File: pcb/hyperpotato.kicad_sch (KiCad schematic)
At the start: 60 parts, among them J1 Conn_01x02_Socket, J2 Conn_01x02_Socket, J3 Conn_01x04, J4 Conn_01x04, J6 Conn_01x12_Socket, K1 SW_Push, K10 SW_Push, K11 SW_Push, K12 SW_Push, K13 SW_Push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

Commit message: WIP re-layout
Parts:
- K1, K10, K11, K12, K13, K14, K16, K17, K2, K3, K4, K6, K7, K8: footprint hyperpotato:PG1350_HS_reversible_plated -> hyperpotato:V1_V2_HS_reversible_plated; symbol Switch:SW_Push -> hyperpotato:SW_Push
- K15: footprint hyperpotato:PG1350_HS_reversible_plated -> hyperpotato:V1_V2_HS_reversible_plated_alt; symbol Switch:SW_Push -> hyperpotato:SW_Push
- K5, K9: footprint hyperpotato:PG1350_reversible_side -> hyperpotato:V1_V2_HS_reversible_plated; symbol Switch:SW_Push -> hyperpotato:SW_Push
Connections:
- net COL3: now also K9.1; no longer K9.2
- net COL4: now also K15.2; no longer K15.1
- net ROW0: now also K1.3, K2.3, K3.3, K4.3, K5.3
- net ROW1: now also K10.3, K6.3, K7.3, K8.3, K9.3
- net ROW2: now also K11.3, K12.3, K13.3, K14.3, K15.3
- net ROW3: now also K16.3, K17.3
- net TP_CLK: now also J6.8 (Pin_8); no longer J6.6 (Pin_6)
- net TP_DATA: now also J6.2 (Pin_2); no longer J6.1 (Pin_1)
- net TP_PCB_RESET: now also J6.3 (Pin_3); no longer J6.2 (Pin_2)
- net VCC: now also J6.1 (Pin_1); no longer J6.8 (Pin_8)
- net at D15.2 (A): now also K15.1; no longer K15.2
- net at D9.2 (A): now also K9.2; no longer K9.1

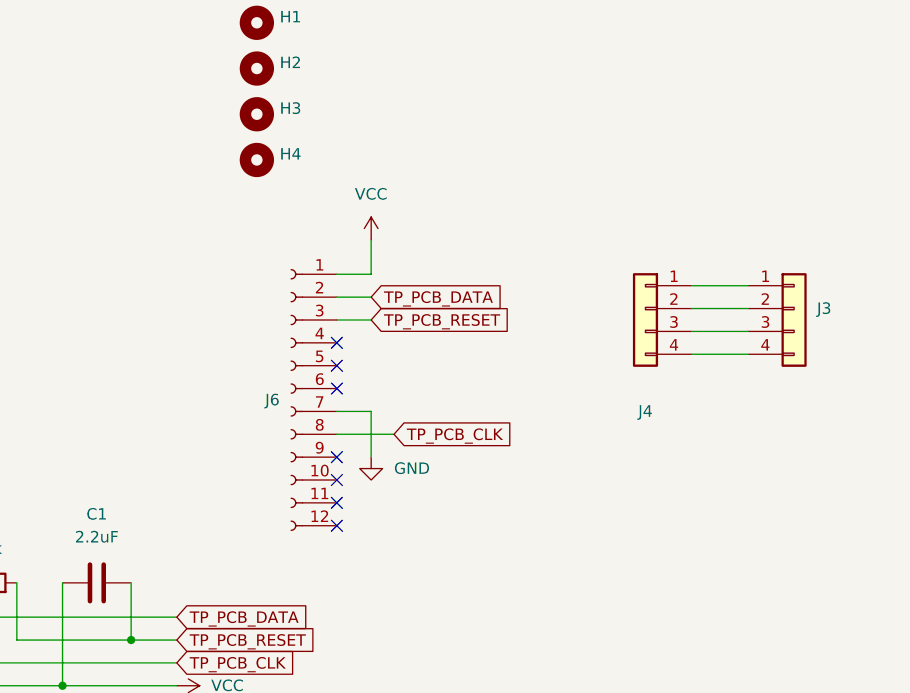
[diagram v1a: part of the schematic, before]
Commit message: WIP trackpoint mounting
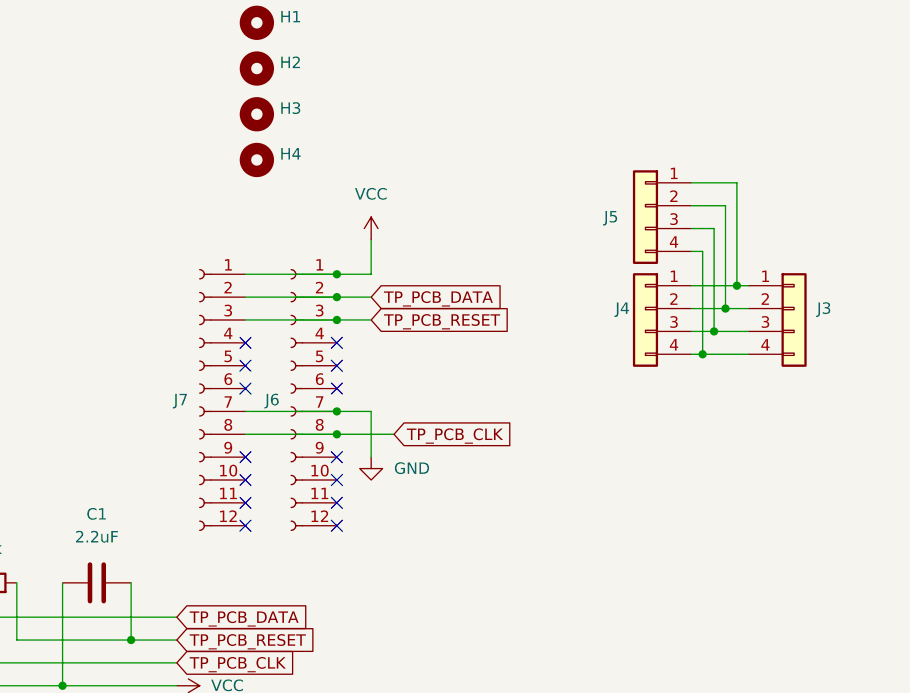
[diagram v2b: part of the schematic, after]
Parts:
- added J5: Conn_01x04, hyperpotato:Trackpoint_Connector, symbol Connector_Generic:Conn_01x04
- added J7: Conn_01x12_Socket, hyperpotato:Trackpoint_PCB_Connector, symbol Connector:Conn_01x12_Socket
- J3: footprint hyperpotato:Trackpoint_Connector -> hyperpotato:Trackpoint_Connector_Reversible
- J4: footprint hyperpotato:Trackponit_PCB -> hyperpotato:Trackpoint_Connector
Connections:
- net GND: now also J7.7 (Pin_7)
- net TP_CLK: now also J7.8 (Pin_8)
- net TP_DATA: now also J7.2 (Pin_2)
- net TP_PCB_RESET: now also J7.3 (Pin_3)
- net VCC: now also J7.1 (Pin_1)
- net at J3.1 (Pin_1), J4.1 (Pin_1): now also J5.1 (Pin_1)
- net at J3.2 (Pin_2), J4.2 (Pin_2): now also J5.2 (Pin_2)
- net at J3.3 (Pin_3), J4.3 (Pin_3): now also J5.3 (Pin_3)
- net at J3.4 (Pin_4), J4.4 (Pin_4): now also J5.4 (Pin_4)
- no-connect marks 10 -> 17
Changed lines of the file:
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@@
 (kicad_sch (version 20230121) (generator eeschema)
   (paper "A4")
+  (junction (at 100.33 149.86) (diameter 0) (color 0 0 0 0)
+  )
   (junction (at 245.11 41.91) (diameter 0) (color 0 0 0 0)
   )
   (junction (at 68.58 48.26) (diameter 0) (color 0 0 0 0)
   )
+  (junction (at 100.33 144.78) (diameter 0) (color 0 0 0 0)
+  )
   (junction (at 86.36 78.74) (diameter 0) (color 0 0 0 0)
   )
@@
   (junction (at 81.28 60.96) (diameter 0) (color 0 0 0 0)
   )
+  (junction (at 140.97 153.67) (diameter 0) (color 0 0 0 0)
+  )
   (junction (at 73.66 40.64) (diameter 0) (color 0 0 0 0)
   )
+  (junction (at 144.78 146.05) (diameter 0) (color 0 0 0 0)
+  )
   (junction (at 40.64 53.34) (diameter 0) (color 0 0 0 0)
   )
@@
   (junction (at 31.75 187.96) (diameter 0) (color 0 0 0 0)
   )
+  (junction (at 100.33 147.32) (diameter 0) (color 0 0 0 0)
+  )
   (junction (at 30.48 48.26) (diameter 0) (color 0 0 0 0)
   )
   (junction (at 86.36 66.04) (diameter 0) (color 0 0 0 0)
   )
+  (junction (at 100.33 160.02) (diameter 0) (color 0 0 0 0)
+  )
   (junction (at 53.34 40.64) (diameter 0) (color 0 0 0 0)
   )
@@
   (junction (at 40.64 40.64) (diameter 0) (color 0 0 0 0)
   )
+  (junction (at 142.24 151.13) (diameter 0) (color 0 0 0 0)
+  )
   (junction (at 68.58 60.96) (diameter 0) (color 0 0 0 0)
   )
@@
   (junction (at 69.85 190.5) (diameter 0) (color 0 0 0 0)
   )
+  (junction (at 143.51 148.59) (diameter 0) (color 0 0 0 0)
+  )
   (junction (at 48.26 40.64) (diameter 0) (color 0 0 0 0)
   )
@@
   (junction (at 73.66 53.34) (diameter 0) (color 0 0 0 0)
   )
+  (junction (at 100.33 162.56) (diameter 0) (color 0 0 0 0)
+  )
   (junction (at 81.28 35.56) (diameter 0) (color 0 0 0 0)
   )
@@
   )
   (no_connect (at 151.13 50.8))
+  (no_connect (at 90.17 154.94))
   (no_connect (at 100.33 172.72))
   (no_connect (at 100.33 154.94))
@@
   (no_connect (at 151.13 48.26))
   (no_connect (at 100.33 152.4))
+  (no_connect (at 90.17 152.4))
+  (no_connect (at 90.17 157.48))
+  (no_connect (at 90.17 170.18))
   (no_connect (at 100.33 165.1))
   (no_connect (at 100.33 167.64))
+  (no_connect (at 90.17 172.72))
   (no_connect (at 229.87 36.83))
   (no_connect (at 100.33 170.18))
+  (no_connect (at 90.17 165.1))
+  (no_connect (at 90.17 167.64))
   (wire (pts (xy 31.75 179.07) (xy 31.75 187.96))
     (stroke (width 0) (type default))
@@
     (stroke (width 0) (type default))
   )
+  (wire (pts (xy 90.17 147.32) (xy 100.33 147.32))
+    (stroke (width 0) (type default))
+  )
   (wire (pts (xy 69.85 179.07) (xy 69.85 190.5))
     (stroke (width 0) (type default))
@@
     (stroke (width 0) (type default))
   )
+  (wire (pts (xy 90.17 160.02) (xy 100.33 160.02))
+    (stroke (width 0) (type default))
+  )
   (wire (pts (xy 43.18 27.94) (xy 43.18 35.56))
     (stroke (width 0) (type default))
@@
     (stroke (width 0) (type default))
   )
+  (wire (pts (xy 140.97 153.67) (xy 146.05 153.67))
+    (stroke (width 0) (type default))
+  )
   (polyline (pts (xy 207.01 17.78) (xy 278.13 17.78))
     (stroke (width 0) (type default))
@@
     (stroke (width 0) (type default))
   )
+  (wire (pts (xy 139.7 139.7) (xy 142.24 139.7))
+    (stroke (width 0) (type default))
+  )
   (wire (pts (xy 123.19 93.98) (xy 130.81 93.98))
     (stroke (width 0) (type default))
@@
     (stroke (width 0) (type default))
   )
-  (wire (pts (xy 139.7 153.67) (xy 146.05 153.67))
+  (wire (pts (xy 139.7 153.67) (xy 140.97 153.67))
     (stroke (width 0) (type default))
   )
@@
     (stroke (width 0) (type default))
   )
+  (wire (pts (xy 140.97 142.24) (xy 140.97 153.67))
+    (stroke (width 0) (type default))
+  )
   (wire (pts (xy 35.56 40.64) (xy 40.64 40.64))
     (stroke (width 0) (type default))
@@
     (stroke (width 0) (type default))
   )
+  (wire (pts (xy 142.24 151.13) (xy 146.05 151.13))
+    (stroke (width 0) (type default))
+  )
+  (wire (pts (xy 144.78 146.05) (xy 146.05 146.05))
+    (stroke (width 0) (type default))
+  )
+  (wire (pts (xy 139.7 142.24) (xy 140.97 142.24))
+    (stroke (width 0) (type default))
+  )
   (polyline (pts (xy 278.13 17.78) (xy 278.13 71.12))
     (stroke (width 0) (type default))
   )
-  (wire (pts (xy 139.7 148.59) (xy 146.05 148.59))
+  (wire (pts (xy 139.7 148.59) (xy 143.51 148.59))
     (stroke (width 0) (type default))
   )
@@
     (stroke (width 0) (type default))
   )
+  (wire (pts (xy 144.78 134.62) (xy 144.78 146.05))
+    (stroke (width 0) (type default))
+  )
   (wire (pts (xy 256.54 57.15) (xy 259.08 57.15))
     (stroke (width 0) (type default))
@@
     (stroke (width 0) (type default))
   )
+  (wire (pts (xy 143.51 137.16) (xy 143.51 148.59))
+    (stroke (width 0) (type default))
+  )
   (wire (pts (xy 26.67 53.34) (xy 35.56 53.34))
     (stroke (width 0) (type default))
@@
     (stroke (width 0) (type default))
   )
-  (wire (pts (xy 139.7 146.05) (xy 146.05 146.05))
+  (wire (pts (xy 139.7 146.05) (xy 144.78 146.05))
     (stroke (width 0) (type default))
   )
@@
     (stroke (width 0) (type default))
   )
+  (wire (pts (xy 90.17 149.86) (xy 100.33 149.86))
+    (stroke (width 0) (type default))
+  )
   (wire (pts (xy 68.58 35.56) (xy 68.58 48.26))
     (stroke (width 0) (type default))
@@
     (stroke (width 0) (type default))
   )
+  (wire (pts (xy 139.7 134.62) (xy 144.78 134.62))
+    (stroke (width 0) (type default))
+  )
   (wire (pts (xy 73.66 66.04) (xy 78.74 66.04))
     (stroke (width 0) (type default))
@@
     (stroke (width 0) (type default))
   )
+  (wire (pts (xy 142.24 139.7) (xy 142.24 151.13))
+    (stroke (width 0) (type default))
+  )
   (wire (pts (xy 198.12 35.56) (xy 198.12 38.1))
     (stroke (width 0) (type default))
@@
     (stroke (width 0) (type default))
   )
+  (wire (pts (xy 143.51 148.59) (xy 146.05 148.59))
+    (stroke (width 0) (type default))
+  )
   (wire (pts (xy 86.36 78.74) (xy 91.44 78.74))
     (stroke (width 0) (type default))
@@
     (stroke (width 0) (type default))
   )
-  (wire (pts (xy 139.7 151.13) (xy 146.05 151.13))
+  (wire (pts (xy 139.7 151.13) (xy 142.24 151.13))
     (stroke (width 0) (type default))
   )
@@
     (stroke (width 0) (type default))
   )
+  (wire (pts (xy 90.17 162.56) (xy 100.33 162.56))
+    (stroke (width 0) (type default))
+  )
   (wire (pts (xy 35.56 66.04) (xy 40.64 66.04))
     (stroke (width 0) (type default))
   )
+  (wire (pts (xy 139.7 137.16) (xy 143.51 137.16))
+    (stroke (width 0) (type default))
+  )
   (wire (pts (xy 245.11 57.15) (xy 245.11 52.07))
     (stroke (width 0) (type default))
@@
   )
   (wire (pts (xy 266.7 41.91) (xy 266.7 59.69))
+    (stroke (width 0) (type default))
+  )
+  (wire (pts (xy 90.17 144.78) (xy 100.33 144.78))
     (stroke (width 0) (type default))
   )
@@
       (effects (font (size 1.27 1.27)) (justify left) hide)
     )
-    (property "Footprint" "hyperpotato:Trackpoint_Connector" (at 151.13 148.59 0)
+    (property "Footprint" "hyperpotato:Trackpoint_Connector_Reversible" (at 151.13 148.59 0)
       (effects (font (size 1.27 1.27)) hide)
     )
@@
     )
   )
+  (symbol (lib_id "Connector_Generic:Conn_01x04") (at 134.62 137.16 0) (mirror y) (unit 1)
+    (in_bom yes) (on_board yes) (dnp no)
+    (property "Reference" "J5" (at 130.81 138.43 0)
+      (effects (font (size 1.27 1.27)))
+    )
+    (property "Value" "Conn_01x04" (at 134.62 146.05 0)
+      (effects (font (size 1.27 1.27)) hide)
+    )
+    (property "Footprint" "hyperpotato:Trackpoint_Connector" (at 134.62 137.16 0)
+      (effects (font (size 1.27 1.27)) hide)
+    )
+    (property "Datasheet" "~" (at 134.62 137.16 0)
+      (effects (font (size 1.27 1.27)) hide)
+    )
+    (pin "2")
+    (pin "3")
+    (pin "4")
+    (pin "1")
+    (instances
+      (project "hyperpotato"
+        (path "/65ee64f1-4704-447d-a409-ecee33d9a68d"
+          (reference "J5") (unit 1)
+        )
+      )
+    )
+  )
   (symbol (lib_id "power:GND") (at 248.92 93.98 90) (unit 1)
     (in_bom yes) (on_board yes) (dnp no) (fields_autoplaced)
@@
         (path "/65ee64f1-4704-447d-a409-ecee33d9a68d"
           (reference "K14") (unit 1)
+        )
+      )
+    )
+  )
+  (symbol (lib_id "Connector:Conn_01x12_Socket") (at 85.09 157.48 0) (mirror y) (unit 1)
+    (in_bom yes) (on_board yes) (dnp no) (fields_autoplaced)
+    (property "Reference" "J7" (at 83.82 158.75 0)
+      (effects (font (size 1.27 1.27)) (justify left))
+    )
+    (property "Value" "Conn_01x12_Socket" (at 83.82 160.02 0)
+      (effects (font (size 1.27 1.27)) (justify left) hide)
+    )
+    (property "Footprint" "hyperpotato:Trackpoint_PCB_Connector" (at 85.09 157.48 0)
+      (effects (font (size 1.27 1.27)) hide)
+    )
+    (property "Datasheet" "~" (at 85.09 157.48 0)
+      (effects (font (size 1.27 1.27)) hide)
+    )
+    (pin "8")
+    (pin "1")
+    (pin "10")
+    (pin "3")
+    (pin "4")
+    (pin "5")
+    (pin "12")
+    (pin "9")
+    (pin "6")
+    (pin "7")
+    (pin "2")
+    (pin "11")
+    (instances
+      (project "hyperpotato"
+        (path "/65ee64f1-4704-447d-a409-ecee33d9a68d"
+          (reference "J7") (unit 1)
         )
       )
@@
   )
   (symbol (lib_id "Connector_Generic:Conn_01x04") (at 134.62 148.59 0) (mirror y) (unit 1)
-    (in_bom yes) (on_board yes) (dnp no) (fields_autoplaced)
-    (property "Reference" "J4" (at 134.62 160.02 0)
+    (in_bom yes) (on_board yes) (dnp no)
+    (property "Reference" "J4" (at 132.08 148.59 0)
       (effects (font (size 1.27 1.27)))
     )
@@
       (effects (font (size 1.27 1.27)) hide)
     )
-    (property "Footprint" "hyperpotato:Trackponit_PCB" (at 134.62 148.59 0)
-      (effects (font (size 1.27 1.27)) hide)
-    )
+    (property "Footprint" "hyperpotato:Trackpoint_Connector" (at 134.62 148.59 0)
+      (effects (font (size 1.27 1.27)) hide)
+    )

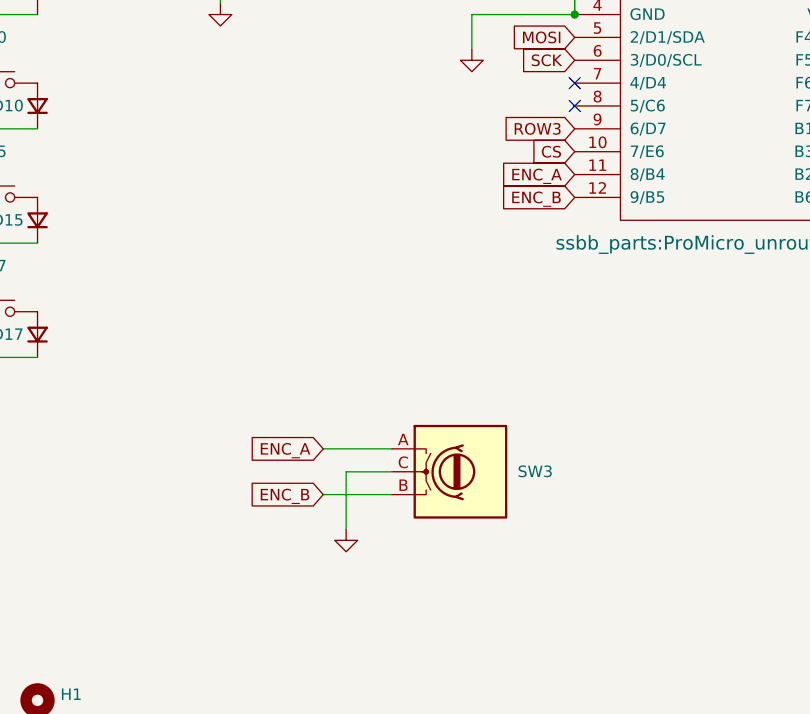
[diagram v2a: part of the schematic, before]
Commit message: Remove encoder
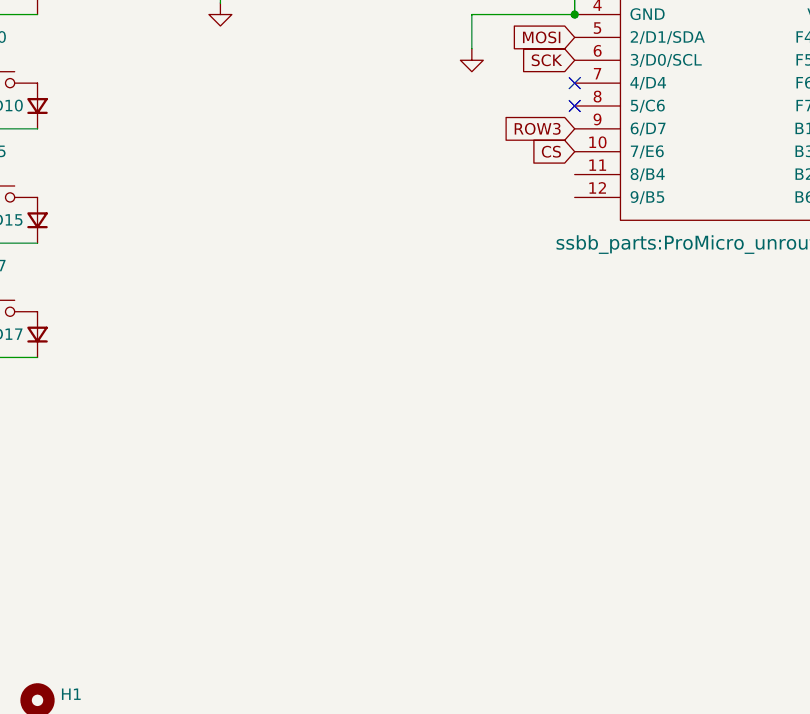
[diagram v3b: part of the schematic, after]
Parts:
- removed SW3: RotaryEncoder, hyperpotato:RotaryEncoder_Alps_EC12E_Vertical_H20mm, symbol Device:RotaryEncoder
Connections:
- net ENC_A: no longer names the net of U1.11 (8/B4)
- net ENC_B: no longer names the net of U1.12 (9/B5)
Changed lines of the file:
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@@
-    (stroke (width 0) (type default))
-  )
-  (wire (pts (xy 123.19 93.98) (xy 130.81 93.98))
     (stroke (width 0) (type default))
   )
@@
     (stroke (width 0) (type default))
   )
-  (wire (pts (xy 125.73 91.44) (xy 125.73 97.79))
-    (stroke (width 0) (type default))
-  )
   (wire (pts (xy 151.13 38.1) (xy 151.13 40.64))
     (stroke (width 0) (type default))
@@
     (stroke (width 0) (type default))
   )
-  (wire (pts (xy 130.81 91.44) (xy 125.73 91.44))
-    (stroke (width 0) (type default))
-  )
   (wire (pts (xy 78.74 78.74) (xy 86.36 78.74))
     (stroke (width 0) (type default))
@@
   )
   (wire (pts (xy 229.87 31.75) (xy 232.41 31.75))
-    (stroke (width 0) (type default))
-  )
-  (wire (pts (xy 123.19 88.9) (xy 130.81 88.9))
     (stroke (width 0) (type default))
   )
@@
     )
   )
-  (global_label "ENC_A" (shape input) (at 123.19 88.9 180) (fields_autoplaced)
-    (effects (font (size 1.27 1.27)) (justify right))
-    (property "Intersheetrefs" "${INTERSHEET_REFS}" (at 114.3991 88.9 0)
-      (effects (font (size 1.27 1.27)) (justify right) hide)
-    )
-  )
   (global_label "DISP_MOSI{slash}CS" (shape input) (at 208.28 106.68 270) (fields_autoplaced)
     (effects (font (size 1.27 1.27)) (justify right))
@@
     )
   )
-  (global_label "ENC_B" (shape input) (at 151.13 60.96 180) (fields_autoplaced)
-    (effects (font (size 1.27 1.27)) (justify right))
-    (property "Intersheetrefs" "${INTERSHEET_REFS}" (at 142.1577 60.96 0)
-      (effects (font (size 1.27 1.27)) (justify right) hide)
-    )
-  )
   (global_label "COL0" (shape input) (at 186.69 53.34 0) (fields_autoplaced)
     (effects (font (size 1.27 1.27)) (justify left))
@@
     )
   )
-  (global_label "ENC_B" (shape input) (at 123.19 93.98 180) (fields_autoplaced)
-    (effects (font (size 1.27 1.27)) (justify right))
-    (property "Intersheetrefs" "${INTERSHEET_REFS}" (at 114.2177 93.98 0)
-      (effects (font (size 1.27 1.27)) (justify right) hide)
-    )
-  )
   (global_label "COL4" (shape input) (at 81.28 27.94 90) (fields_autoplaced)
     (effects (font (size 1.27 1.27)) (justify left))
@@
     (property "Intersheetrefs" "${INTERSHEET_REFS}" (at 256.422 114.3 0)
       (effects (font (size 1.27 1.27)) (justify left) hide)
-    )
-  )
-  (global_label "ENC_A" (shape input) (at 151.13 58.42 180) (fields_autoplaced)
-    (effects (font (size 1.27 1.27)) (justify right))
-    (property "Intersheetrefs" "${INTERSHEET_REFS}" (at 142.3391 58.42 0)
-      (effects (font (size 1.27 1.27)) (justify right) hide)
     )
   )
@@
         (path "/65ee64f1-4704-447d-a409-ecee33d9a68d"
           (reference "K11") (unit 1)
-        )
-      )
-    )
-  )
-  (symbol (lib_id "Device:RotaryEncoder") (at 138.43 91.44 0) (unit 1)
-    (in_bom yes) (on_board yes) (dnp no) (fields_autoplaced)
-    (property "Reference" "SW3" (at 144.78 91.44 0)
-      (effects (font (size 1.27 1.27)) (justify left))
-    )
-    (property "Value" "RotaryEncoder" (at 144.78 92.71 0)
-      (effects (font (size 1.27 1.27)) (justify left) hide)
-    )
-    (property "Footprint" "hyperpotato:RotaryEncoder_Alps_EC12E_Vertical_H20mm" (at 134.62 87.376 0)
-      (effects (font (size 1.27 1.27)) hide)
-    )
-    (property "Datasheet" "~" (at 138.43 84.836 0)
-      (effects (font (size 1.27 1.27)) hide)
-    )
-    (pin "A")
-    (pin "B")
-    (pin "C")
-    (instances
-      (project "hyperpotato"
-        (path "/65ee64f1-4704-447d-a409-ecee33d9a68d"
-          (reference "SW3") (unit 1)
         )
       )
@@
         )
       )
-    )
-  )
-  (symbol (lib_id "power:GND") (at 125.73 97.79 0) (unit 1)
-    (in_bom yes) (on_board yes) (dnp no) (fields_autoplaced)
-    (property "Reference" "#PWR04" (at 125.73 104.14 0)
-      (effects (font (size 1.27 1.27)) hide)
-    )
-    (property "Value" "GND" (at 125.73 102.87 0)
-      (effects (font (size 1.27 1.27)) hide)
-    )
-    (property "Footprint" "" (at 125.73 97.79 0)
-      (effects (font (size 1.27 1.27)) hide)
-    )
-    (property "Datasheet" "" (at 125.73 97.79 0)
-      (effects (font (size 1.27 1.27)) hide)
-    )
-    (pin "1")
-    (instances
-      (project "hyperpotato"
-        (path "/65ee64f1-4704-447d-a409-ecee33d9a68d"
-          (reference "#PWR04") (unit 1)
-        )
-      )
